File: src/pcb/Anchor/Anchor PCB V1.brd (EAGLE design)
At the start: 100 x 80 mm, 17 parts, among them Q1 48 MHz, U1 ATSAMD21G-A, X1 MINI-USB-UX60-MB-5ST

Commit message: Completed schematic anchor with PoE
PCB design has not been done yet.
Changes might happen in the future
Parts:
- added 10-PIN-PROGRAMMER: (no value), con-lsta:FE05-2
- added BR1, BR2: HD04-T, HD04-T:SOP250P700X270-4N
- added C10: 560 pF, rcl:C0805
- added C11: 15 pF, rcl:C0805
- added C12: 33 nF, rcl:C0805
- added C13: 47 µF (63V), rcl:B45181D
- added C14, C15: 1 µF (100V), rcl:C0805
- added C16: 1 µF (16V), rcl:C0805
- added C17: 0.22 µF (10V), rcl:C0805
- added C18: 0.1 µF, rcl:C0805
- added C19, C20, C21: 10 µF (6.3V), rcl:C0805
- added C22, C24: 10 µF, rcl:E5-5
- added C23: 100 µF (6.3V), rcl:UD-5X5,8_NICHICON
- added C25, C26: 100 nF, rcl:C0805
- added C27: 10 µF, rcl:C0805
- added C28, C29: 18 µF, rcl:C0805
- added C9: 0.1 µF (100V), rcl:C0805
- added D1: SMAJ58A, SMAJ58A:DIOM5026X229N
- added D2: 6CWQ10FN, shottky:DPAK
- added D3: POWER, SparkFun-LED:LED-1206
- added D4, D6: TX, SparkFun-LED:LED-1206
- added D5, D7: RX, SparkFun-LED:LED-1206
- added IC2: TPS23750PWP, TPS23750PWP:SOP65P640X120-21N
- added IC3: REG1117, burr-brown:SOT223
- added IC4: DWM1000, DWM1000:DWM1000
- added J1: 0826-1X1T-GJ-F, 0826-1X1T-GJ-F:0826-1X1T-GJ-F
- added JP1: (no value), jumper:JP1
- added L1: FB_1206, rc-master-smd:L1206
- added L1(74437336100): 10 µH, inductors:DR73
- added L2: 33 µH, inductors:DR73
- added Q2: SUD06N10-225L, transistor-power:SOT223
- added R10: 10 Ω, rcl:R0805
- added R11: 1.5 kΩ, rcl:R0805
- added R12: 3.48 kΩ, rcl:R0805
- added R13: 51.1 Ω, rcl:R0805
- added R14, R28: 270 Ω, rcl:R0805
- added R15, R16, R17, R18: 49.9 Ω, rcl:R0805
- added R19: 2.32 kΩ 1%, rcl:R0805
- added R20, R21, R22: 330 Ω, rcl:R0805
- added R23: 1 kΩ, rcl:R0805
- added R24, R25: 100 Ω, rcl:R0805
- added R26, R29: 220 Ω, rcl:R0805
- added R27: 10 kΩ, rcl:M0805
- added R5: 24,9 kΩ, rcl:R0805
- added R6: 100 kΩ, rcl:R0805
- added R7: 357 Ω (0.25W), rcl:R0805
- added R8: 75 kΩ, rcl:R0805
- added R9: 0.18 mΩ (0.5W), rcl:R0805
- added Y1: 25 MHz, SparkFun-Clocks:HC49UP
- C7: device rcl:E7,5-18 -> rcl:E5-5
- C8: device rcl:E7,5-18 -> rcl:E5-4
- IC1: value (none) -> ENC28J60-I_SS; device v-reg:317TL -> ENC28J60-I_SS:SOP65P780X200-28N
- R2: value 390 Ω -> 443 Ω
- R3: value 47 Ω -> 470 Ω; device rcl:M0805 -> rcl:R0805
- S1: device SparkFun-Switches:TACTILE_SWITCH_PTH_6.0MM_KIT -> SparkFun-Switches:TACTILE_SWITCH_SMD_4.5MM
- moved R3 407.4 mm to (-212.1, -368.3)
- moved IC1 289.8 mm to (-182.9, -223.5)
- moved C7 161.0 mm to (-2.54, -188.9)
- moved C8 154.6 mm to (-2.54, -201.6)
- moved R4 121.7 mm to (-59.7, 55.9)
- moved S1 108.5 mm to (-2.23, -174.5)
- moved X1 85.9 mm to (-52.1, 30.5)
- moved R2 78.6 mm to (-53.3, 55.9)
- moved R1 70.8 mm to (-47.0, 55.9)
- moved C1 69.4 mm to (-55.9, 44.5)
- moved Q1 63.6 mm to (-38.1, 45.7)
- moved C2 59.5 mm to (-17.8, 55.9)
- moved C6 54.0 mm to (-40.6, 55.9)
- moved U1 53.9 mm to (-27.9, 47.0)
- moved C4 46.2 mm to (-25.4, 55.9)
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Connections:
- new net 1_VC+: BR1.4, J1.7
- new net 1_VC-: BR1.3, J1.8
- new net 2_VC+: BR2.4, J1.9
- new net 2_VC-: BR2.3, J1.10
- new net AUX: C16.1, IC2.16
- new net COMP: C11.2, IC2.3, R6.2
- new net COM_A_SHTKY: D2.1, D2.3, L2.1, Q2.4
- new net CS1: IC1.9
- new net CSN_DWM: IC4.17, U1.27
- new net FB: C10.1, C11.1, IC2.2
- new net FREQ: IC2.20, R8.2
- new net GATE: IC2.15, R10.1
- new net GRN_CAT: J1.13, R24.1
- new net GRN_LED: IC1.26, J1.14
- new net IRQ: IC4.22, R27.2
- new net MISO1_MC: R20.1, U1.21
- new net MISO2_MC: IC4.19, U1.28
- new net MOSI1_MC: R21.1, U1.19
- new net MOSI2_MC: IC4.18, U1.25
- new net N$10: R12.1, R13.2
- new net N$11: D4.A, R14.1
- new net N$12: D5.A, R26.1
- new net N$13: D6.A, R28.1
- new net N$14: D7.A, R29.1
- new net N$9: D3.A, R3.1
- new net OSC1: C28.1, IC1.23, Y1.1
- new net OSC2: C29.1, IC1.24, Y1.2
- new net POE+: BR1.1, BR2.1, C13.+, C9.1, D1.1, IC2.7, L1(74437336100).1, R5.2
- new net REG_GND: C22.+, IC3.1, R1.1, R2.2
- new net RSP: IC2.12, Q2.3, R9.2
- new net RST_DWM: IC4.3, U1.29
- new net RTN: C12.2, C13.-, C14.2, C15.2, C16.2, C17.2, IC2.11, IC2.13, IC2.14, IC2.17, IC2.19, R8.1, R9.1
- new net RXLED_DWM: D7.C, IC4.13
- new net RX_MC: D5.C, U1.16, U1.38
- new net SCK1_MC: R22.1, U1.20
- new net SCK2_MC: IC4.20, U1.26
- new net SCK_ETH: IC1.8, R22.2
- new net SEN: C18.1, IC2.4, R11.1, R12.2
- new net SI_ETH: IC1.7, R21.2
- new net SO_ETH: IC1.6, R20.2
- new net SWCLK: 10-PIN-PROGRAMMER.4, R23.1, U1.45
- new net SWDIO: 10-PIN-PROGRAMMER.2, U1.46
- new net SWO: 10-PIN-PROGRAMMER.6
- new net TMR: C12.1, IC2.1
- new net TPIN+: IC1.13, J1.1, R17.1
- new net TPIN-: IC1.12, J1.2, R18.2
- new net TPOUT+: IC1.17, J1.5, R15.1
- new net TPOUT-: IC1.16, J1.4, R16.2
- new net TXLED_DWM: D6.C, IC4.12
- new net TX_MC: D4.C, U1.15, U1.37
- new net VBIAS: C17.1, IC2.18
- new net VBUS: X1.1
- new net VCAP: C27.1, IC1.1
- new net VOUT+: C14.1, C15.1, C19.1, C20.1, C21.1, C23.+, C24.+, D2.4, IC2.6, IC3.3, JP1.1, L1(74437336100).2, R11.2
- new net YEL_CAT: J1.11, R25.1
- new net YEL_LED: IC1.27, J1.12
- net GND: now also 10-PIN-PROGRAMMER.3, 10-PIN-PROGRAMMER.5, 10-PIN-PROGRAMMER.9, BR1.2, BR2.2, C18.2, C19.2, C20.2, C21.2, C22.-, C23.-, C24.-, C25.2, C26.2, C27.2, C28.2, C29.2, C9.2, D1.2, D3.C, IC1.11, IC1.18, IC1.2, IC1.21, IC1.22, IC2.10, IC2.21, IC4.16, IC4.21, IC4.23, IC4.24, IC4.8, JP1.2, L2.2, R13.1, R19.2, R2.1, R24.2, R25.2, R27.1, R7.1, S1.2, S1.3; no longer R3.1, S1.1
- net N$2: now also IC2.8, R5.1; no longer C5.1, Q1.3
- net N$3: now also IC2.9, R7.2; no longer C6.1, Q1.1
- net N$4: now also C25.1, J1.6, L1.1, R15.2, R16.1; no longer IC1.1, R1.1, R2.2
- net N$5: now also C10.2, R6.1; no longer X1.3
- net N$6: now also C26.1, J1.3, R17.2, R18.1; no longer R2.1, R3.2
- net N$7: now also Q2.1, R10.2; no longer X1.2
- net N$8: now also IC1.14, R19.1; no longer R4.1, S1.3
- net RESET: now also 10-PIN-PROGRAMMER.10, R4.1, S1.1, S1.4
- net USB+: now also X1.3
- net USB-: now also X1.2
- net VCC: now also 10-PIN-PROGRAMMER.1, IC1.10, IC1.15, IC1.19, IC1.20, IC1.25, IC1.28, IC3.2, IC4.5, IC4.6, L1.2, R14.2, R23.2, R26.2, R28.2, R29.2, R3.2; no longer IC1.2, IC1.3, X1.1
- net XTAL1: now also C5.1, Q1.3
- net XTAL2: now also C6.1, Q1.1

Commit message: Updated capacitor values XTAL
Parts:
- C28, C29: value 18 µF -> 18 pF
- C5, C6: value 100 nF -> 18 pF
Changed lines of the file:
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@@
 <attribute name="VALUE" x="-26.67" y="53.34" size="1.27" layer="27"/>
 </element>
-<element name="C5" library="rcl" library_urn="urn:adsk.eagle:library:334" package="C0805" package3d_urn="urn:adsk.eagle:package:23617/2" value="100 nF" x="-33.02" y="55.88" smashed="yes">
+<element name="C5" library="rcl" library_urn="urn:adsk.eagle:library:334" package="C0805" package3d_urn="urn:adsk.eagle:package:23617/2" value="18 pF" x="-33.02" y="55.88" smashed="yes">
 <attribute name="NAME" x="-34.29" y="57.15" size="1.27" layer="25"/>
 <attribute name="SPICEPREFIX" value="C" x="0" y="0" size="1.778" layer="27" display="off"/>
 <attribute name="VALUE" x="-34.29" y="53.34" size="1.27" layer="27"/>
 </element>
-<element name="C6" library="rcl" library_urn="urn:adsk.eagle:library:334" package="C0805" package3d_urn="urn:adsk.eagle:package:23617/2" value="100 nF" x="-40.64" y="55.88" smashed="yes">
+<element name="C6" library="rcl" library_urn="urn:adsk.eagle:library:334" package="C0805" package3d_urn="urn:adsk.eagle:package:23617/2" value="18 pF" x="-40.64" y="55.88" smashed="yes">
 <attribute name="NAME" x="-41.91" y="57.15" size="1.27" layer="25"/>
 <attribute name="SPICEPREFIX" value="C" x="0" y="0" size="1.778" layer="27" display="off"/>
@@
 <attribute name="VALUE" x="-193.675" y="-289.56" size="1.27" layer="27"/>
 </element>
-<element name="C28" library="rcl" library_urn="urn:adsk.eagle:library:334" package="C0805" package3d_urn="urn:adsk.eagle:package:23617/2" value="18 µF" x="-193.04" y="-293.37" smashed="yes">
+<element name="C28" library="rcl" library_urn="urn:adsk.eagle:library:334" package="C0805" package3d_urn="urn:adsk.eagle:package:23617/2" value="18 pF" x="-193.04" y="-293.37" smashed="yes">
 <attribute name="NAME" x="-194.31" y="-292.1" size="1.27" layer="25"/>
 <attribute name="SPICEPREFIX" value="C" x="-193.04" y="-293.37" size="1.778" layer="27" display="off"/>
 <attribute name="VALUE" x="-194.31" y="-295.91" size="1.27" layer="27"/>
 </element>
-<element name="C29" library="rcl" library_urn="urn:adsk.eagle:library:334" package="C0805" package3d_urn="urn:adsk.eagle:package:23617/2" value="18 µF" x="-193.04" y="-299.72" smashed="yes">
+<element name="C29" library="rcl" library_urn="urn:adsk.eagle:library:334" package="C0805" package3d_urn="urn:adsk.eagle:package:23617/2" value="18 pF" x="-193.04" y="-299.72" smashed="yes">
 <attribute name="NAME" x="-194.31" y="-298.45" size="1.27" layer="25"/>
 <attribute name="SPICEPREFIX" value="C" x="-193.04" y="-299.72" size="1.778" layer="27" display="off"/>

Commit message: First version of PCB layout
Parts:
- removed C22, C24: 10 µF, rcl:E5-5
- removed C7: 100 nF, rcl:E5-5
- removed C8: 1 µF, rcl:E5-4
- removed IC3: REG1117, burr-brown:SOT223
- removed R1: 270 Ω, rcl:M0805
- removed R2: 443 Ω, rcl:M0805
- added C30: 22 µF, rcl:E5-5
- added C31: 0.1 µF, rcl:E5-4
- added D8: 1PS79SB10, nxp_60_1_1:SOD523
- added D9: PRTR5V0U2X,215, PRTR5V0U2X_215:SOT-143B
- added IC5: MIC5209-3.3YS-TR, MIC5209-3.3YS-TR:SOT230P700X170-4N
- added JP2, JP3: (no value), jumper:JP1
- C13: device rcl:B45181D -> rcl:E3,5-8
- Q1: value 48 MHz -> 32 MHz
- R9: device rcl:R0805 -> rcl:R2010
- X1: value MINI-USB-UX60-MB-5ST -> MICRO-USB-RECEPTACLE47589-0001; device con-hirose:UX60-MB-5ST -> con-molex-usb:47589-0001
- moved R27 513.8 mm to (14.7, 56.9), turned to 270 degrees
- moved D6 502.9 mm to (6.86, 31.0), turned to 270 degrees
- moved IC4 501.7 mm to (24.4, 46.2), turned to 90 degrees
- moved R29 501.3 mm to (4.32, 35.6), turned to 90 degrees
- moved D7 499.5 mm to (4.57, 31.0), turned to 270 degrees
- moved R26 498.2 mm to (46.2, 45.0), turned to 90 degrees
- moved R28 496.9 mm to (6.86, 35.6), turned to 90 degrees
- moved R25 495.1 mm to (95.2, 30.0), turned to 90 degrees
- moved R14 494.2 mm to (49.0, 45.0), turned to 90 degrees
- moved R3 490.3 mm to (51.8, 45.0), turned to 90 degrees
- moved R24 483.6 mm to (84.8, 30.0), turned to 90 degrees
- moved D3 482.2 mm to (51.8, 40.4), turned to 270 degrees
- moved D5 479.7 mm to (23.6, 27.9), turned to 270 degrees
- moved D4 477.6 mm to (25.9, 27.9), turned to 270 degrees
- moved J1 427.9 mm to (89.7, -5.33), turned to 180 degrees
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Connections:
- removed net REG_GND: C22.+, IC3.1, R1.1, R2.2
- new net ID: X1.4
- new net N$15: D8.1, D9.4
- net GND: now also C30.-, C31.-, D9.1, IC5.2, IC5.4, JP2.2, JP3.2, X1.CASING1, X1.CASING2, X1.CASING3, X1.CASING4; no longer C22.-, C24.-, C7.-, C8.-, R2.1, X1.4
- net POE+: now also JP3.1
- net USB+: now also D9.2
- net USB-: now also D9.3
- net VBUS: now also D8.2
- net VCC: now also C30.+, IC5.3, JP2.1; no longer C7.+, C8.+, IC3.2, R1.2
- net VOUT+: now also C31.+, IC5.1; no longer C24.+, IC3.3
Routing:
- net GND: track 0.00 -> 567.4 mm, vias 0 -> 2
- net VCC: track 0.00 -> 304.2 mm, vias 0 -> 4
- net VOUT+: track 0.00 -> 107.2 mm, vias 0 -> 3
- net POE+: track 0.00 -> 91.2 mm, vias 0 -> 2
- net RTN: track 0.00 -> 69.7 mm, vias 0 -> 2
- net SO_ETH: track 0.00 -> 61.4 mm, vias 0 -> 2
- net SCK_ETH: track 0.00 -> 58.9 mm, vias 0 -> 2
- net RSP: track 0.00 -> 56.6 mm
- net SI_ETH: track 0.00 -> 55.2 mm, vias 0 -> 2
- net TPOUT+: track 0.00 -> 49.5 mm
- net SCK2_MC: track 0.00 -> 47.7 mm
- net OSC2: track 0.00 -> 45.6 mm, vias 0 -> 2
- net N$6: track 0.00 -> 40.8 mm, vias 0 -> 2
- net TPOUT-: track 0.00 -> 39.1 mm, vias 0 -> 1
- net CSN_DWM: track 0.00 -> 38.6 mm, vias 0 -> 2
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
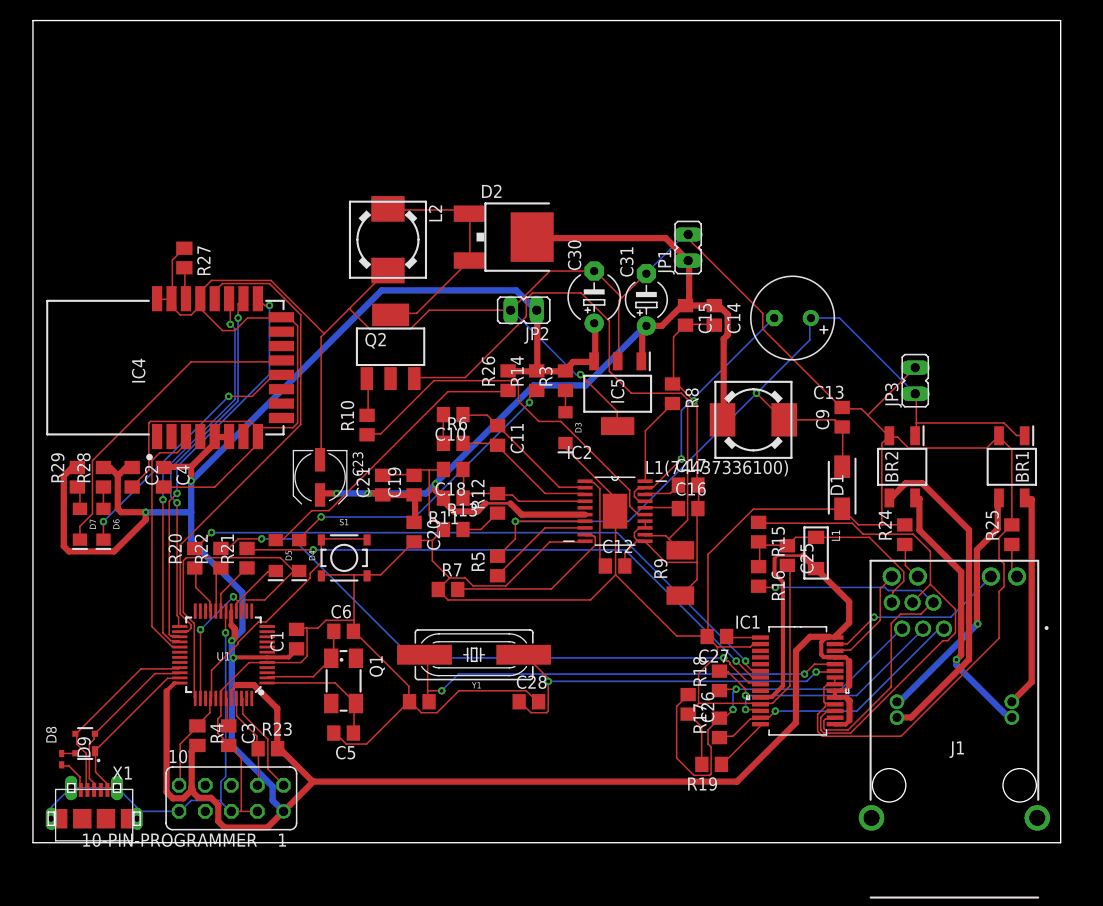
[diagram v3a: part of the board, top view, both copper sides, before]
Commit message: Updating board
Update board so that we are using parts that are available in the labo.
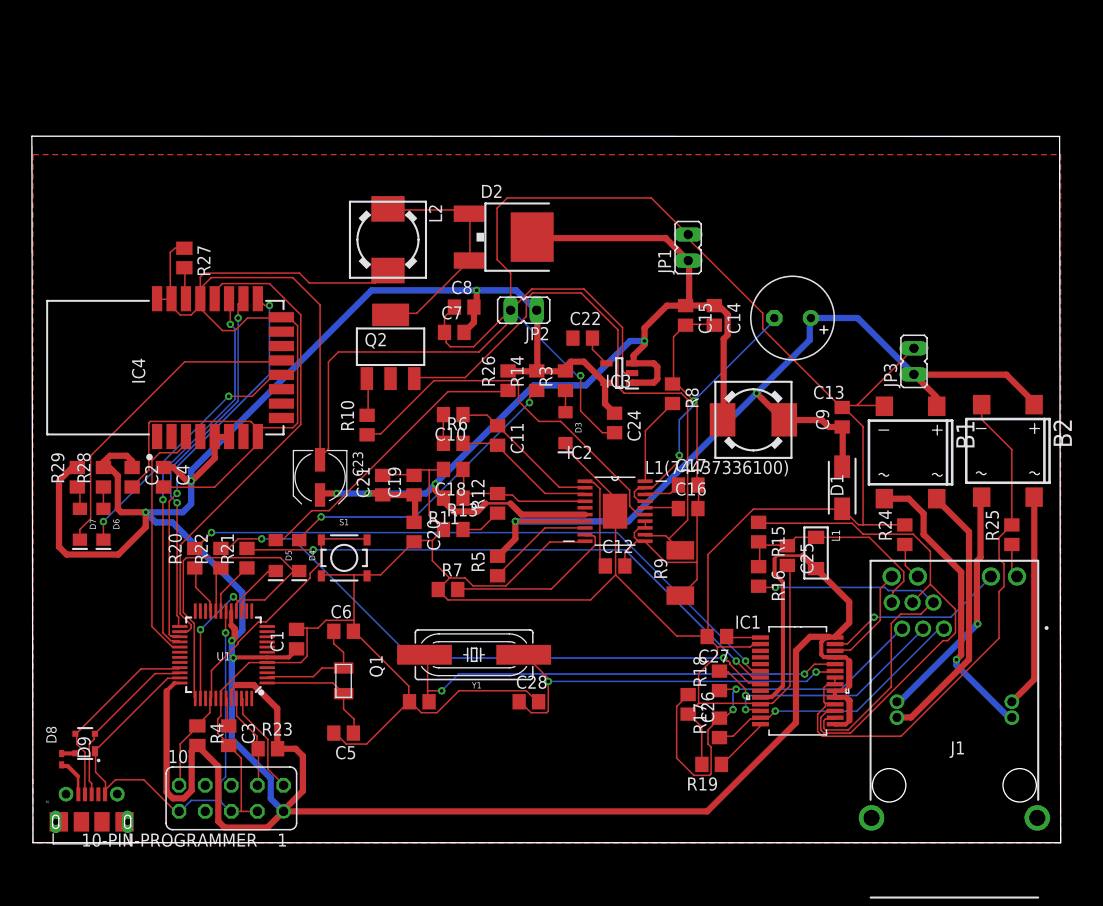
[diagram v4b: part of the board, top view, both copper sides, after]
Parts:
- removed BR1, BR2: HD04-T, HD04-T:SOP250P700X270-4N
- removed C30: 22 µF, rcl:E5-5
- removed C31: 0.1 µF, rcl:E5-4
- removed IC5: MIC5209-3.3YS-TR, MIC5209-3.3YS-TR:SOT230P700X170-4N
- removed X1: MICRO-USB-RECEPTACLE47589-0001, con-molex-usb:47589-0001
- added B1, B2: DBS103G, rectifier:DBS
- added C22: 470 pF, rcl:C0805
- added C24: 2.2 µF, rcl:C0805
- added C7: 100 nF, rcl:C0805
- added C8: 1 µF, rcl:C0805
- added IC3: MIC5219-3.3YM5-TR, MIC5219-3.3YM5-TR:SOT95P280X130-5N
- added J2: 105017-0001, 105017-0001:MOLEX_105017-0001
- Q1: device crystal:CTS406 -> abracon:ABS07
- moved JP3 1.88 mm to (85.7, 46.8)
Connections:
- removed net POE+: BR1.1, BR2.1, C13.+, C9.1, D1.1, IC2.7, JP3.1, L1(74437336100).1, R5.2
- removed net VOUT+: C14.1, C15.1, C19.1, C20.1, C21.1, C23.+, C31.+, D2.4, IC2.6, IC5.1, JP1.1, L1(74437336100).2, R11.2
- new net 48V: B1.+, B2.+, C13.+, C9.1, D1.1, IC2.7, JP3.1, L1(74437336100).1, R5.2
- new net 5V: C14.1, C15.1, C19.1, C20.1, C21.1, C23.+, D2.4, IC2.6, IC3.1, IC3.3, JP1.1, L1(74437336100).2, R11.2
- new net N$18: C22.2, IC3.4
- net 1_VC+: now also B2.AC1; no longer BR1.4
- net 1_VC-: now also B2.AC2; no longer BR1.3
- net 2_VC+: now also B1.AC2; no longer BR2.4
- net 2_VC-: now also B1.AC1; no longer BR2.3
- net GND: now also B1.-, B2.-, C22.1, C24.2, C7.1, C8.1, IC3.2, J2.5; no longer BR1.2, BR2.2, C30.-, C31.-, IC5.2, IC5.4, X1.5, X1.CASING1, X1.CASING2, X1.CASING3, X1.CASING4
- net ID: now also J2.4; no longer X1.4
- net USB+: now also J2.3; no longer X1.3
- net USB-: now also J2.2; no longer X1.2
- net VBUS: now also J2.1; no longer X1.1
- net VCC: now also C24.1, C7.2, C8.2, IC3.5; no longer C30.+, IC5.3
- net XTAL1: now also Q1.2; no longer Q1.3
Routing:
- net 5V: track 0.00 -> 113.3 mm, vias 0 -> 4
- net VOUT+: track 107.2 -> 0.00 mm, vias 3 -> 0
- net 48V: track 0.00 -> 92.1 mm, vias 0 -> 2
- net POE+: track 91.2 -> 0.00 mm, vias 2 -> 0
- net GND: track 567.4 -> 615.6 mm
- net VCC: track 304.2 -> 325.2 mm, vias 4 -> 5
- net 2_VC-: track 32.2 -> 26.2 mm
- net N$18: track 0.00 -> 3.02 mm
- net 2_VC+: track 26.0 -> 28.4 mm
- net XTAL2: track 9.82 -> 11.9 mm
- added copper zone on layer 1, net GND
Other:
- board size 100 x 80 mm -> 100.1 x 68.7 mm

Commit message: Final version of V1
Added ground plane
Some rewiring has been done.
Swapping to MIC5219
Changed USB-port
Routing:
- net 5V: vias 4 -> 6
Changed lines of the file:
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@@
 <wire x1="48.5394" y1="53.8734" x2="53.6194" y2="53.8734" width="0.1524" layer="1"/>
 <wire x1="52.959" y1="45.4406" x2="52.5424" y2="49.0982" width="0" layer="19" extent="1-16"/>
-<wire x1="7.0612" y1="5.1816" x2="7.015" y2="5.11" width="0" layer="19" extent="1-1"/>
-<wire x1="76.962" y1="15.0876" x2="73.66" y2="15.2654" width="0" layer="19" extent="1-1"/>
 </signal>
 <signal name="VCC">
@@
 <contactref element="IC2" pad="1"/>
 <contactref element="C12" pad="1"/>
-<wire x1="54.5592" y1="35.052" x2="53.7972" y2="35.052" width="0.1524" layer="1"/>
-<wire x1="55.1688" y1="34.4424" x2="54.5592" y2="35.052" width="0.1524" layer="1"/>
-<wire x1="55.1688" y1="27.432" x2="55.1688" y2="34.4424" width="0.1524" layer="1"/>
+<wire x1="54.483" y1="35.179" x2="53.721" y2="35.179" width="0.1524" layer="1"/>
+<wire x1="55.1688" y1="34.4932" x2="54.483" y2="35.179" width="0.1524" layer="1"/>
+<wire x1="55.1688" y1="27.432" x2="55.1688" y2="34.4932" width="0.1524" layer="1"/>
 <wire x1="55.626" y1="26.9748" x2="55.1688" y2="27.432" width="0.1524" layer="1"/>
-<wire x1="53.7972" y1="35.052" x2="53.721" y2="35.179" width="0.1524" layer="1"/>
 <wire x1="55.626" y1="26.9748" x2="55.692" y2="26.924" width="0.1524" layer="1"/>
 </signal>
@@
 <wire x1="28.0416" y1="33.9852" x2="27.94" y2="33.835" width="0.6096" layer="1"/>
 <wire x1="33.9852" y1="33.9852" x2="34.036" y2="33.848" width="0.6096" layer="1"/>
-<wire x1="47.5488" y1="31.9278" x2="53.721" y2="31.9278" width="0.6096" layer="1"/>
-<wire x1="46.4566" y1="33.02" x2="47.5488" y2="31.9278" width="0.6096" layer="1"/>
-<wire x1="44.0436" y1="33.02" x2="46.4566" y2="33.02" width="0.254" layer="1"/>
-<wire x1="43.2562" y1="32.2326" x2="44.0436" y2="33.02" width="0.6096" layer="1"/>
-<wire x1="40.9448" y1="32.2326" x2="43.2562" y2="32.2326" width="0.6096" layer="1"/>
+<wire x1="42.8498" y1="32.2326" x2="43.561" y2="32.9438" width="0.6096" layer="1"/>
+<wire x1="40.9448" y1="32.2326" x2="42.8498" y2="32.2326" width="0.6096" layer="1"/>
 <wire x1="40.9448" y1="32.2326" x2="39.944" y2="33.2334" width="0.6096" layer="1"/>
 <wire x1="39.944" y1="33.528" x2="39.944" y2="33.2334" width="0.6096" layer="1"/>
@@
 <wire x1="59.5122" y1="48.8188" x2="58.1152" y2="48.8188" width="0.6096" layer="16"/>
 <wire x1="59.5122" y1="50.0888" x2="59.5122" y2="48.8188" width="0.6096" layer="1"/>
+<via x="43.561" y="32.9438" extent="1-16" drill="0.35"/>
+<via x="46.7868" y="32.5882" extent="1-16" drill="0.35"/>
+<wire x1="46.4058" y1="32.9438" x2="43.561" y2="32.9438" width="0.6096" layer="16"/>
+<wire x1="46.7614" y1="32.5882" x2="46.7868" y2="32.5882" width="0.6096" layer="16"/>
+<wire x1="46.7614" y1="32.5882" x2="46.4058" y2="32.9438" width="0.6096" layer="16"/>
+<wire x1="47.6758" y1="31.9278" x2="47.0154" y2="32.5882" width="0.6096" layer="1"/>
+<wire x1="47.0154" y1="32.5882" x2="46.7868" y2="32.5882" width="0.6096" layer="1"/>
+<wire x1="53.721" y1="31.9278" x2="47.6758" y2="31.9278" width="0.6096" layer="1"/>
 </signal>
 <signal name="VBIAS">
@@
 <wire x1="2.8956" y1="7.4676" x2="2.794" y2="7.578" width="0.1524" layer="1"/>
 <contactref element="J2" pad="1"/>
-<wire x1="4.3942" y1="5.134" x2="4.415" y2="4.707" width="0" layer="19" extent="1-1"/>
+<wire x1="4.415" y1="4.707" x2="4.3942" y2="5.134" width="0" layer="19" extent="1-1"/>
 </signal>
 <signal name="VCAP">
